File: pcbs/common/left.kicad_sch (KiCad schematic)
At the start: 89 parts, among them J2 TRS

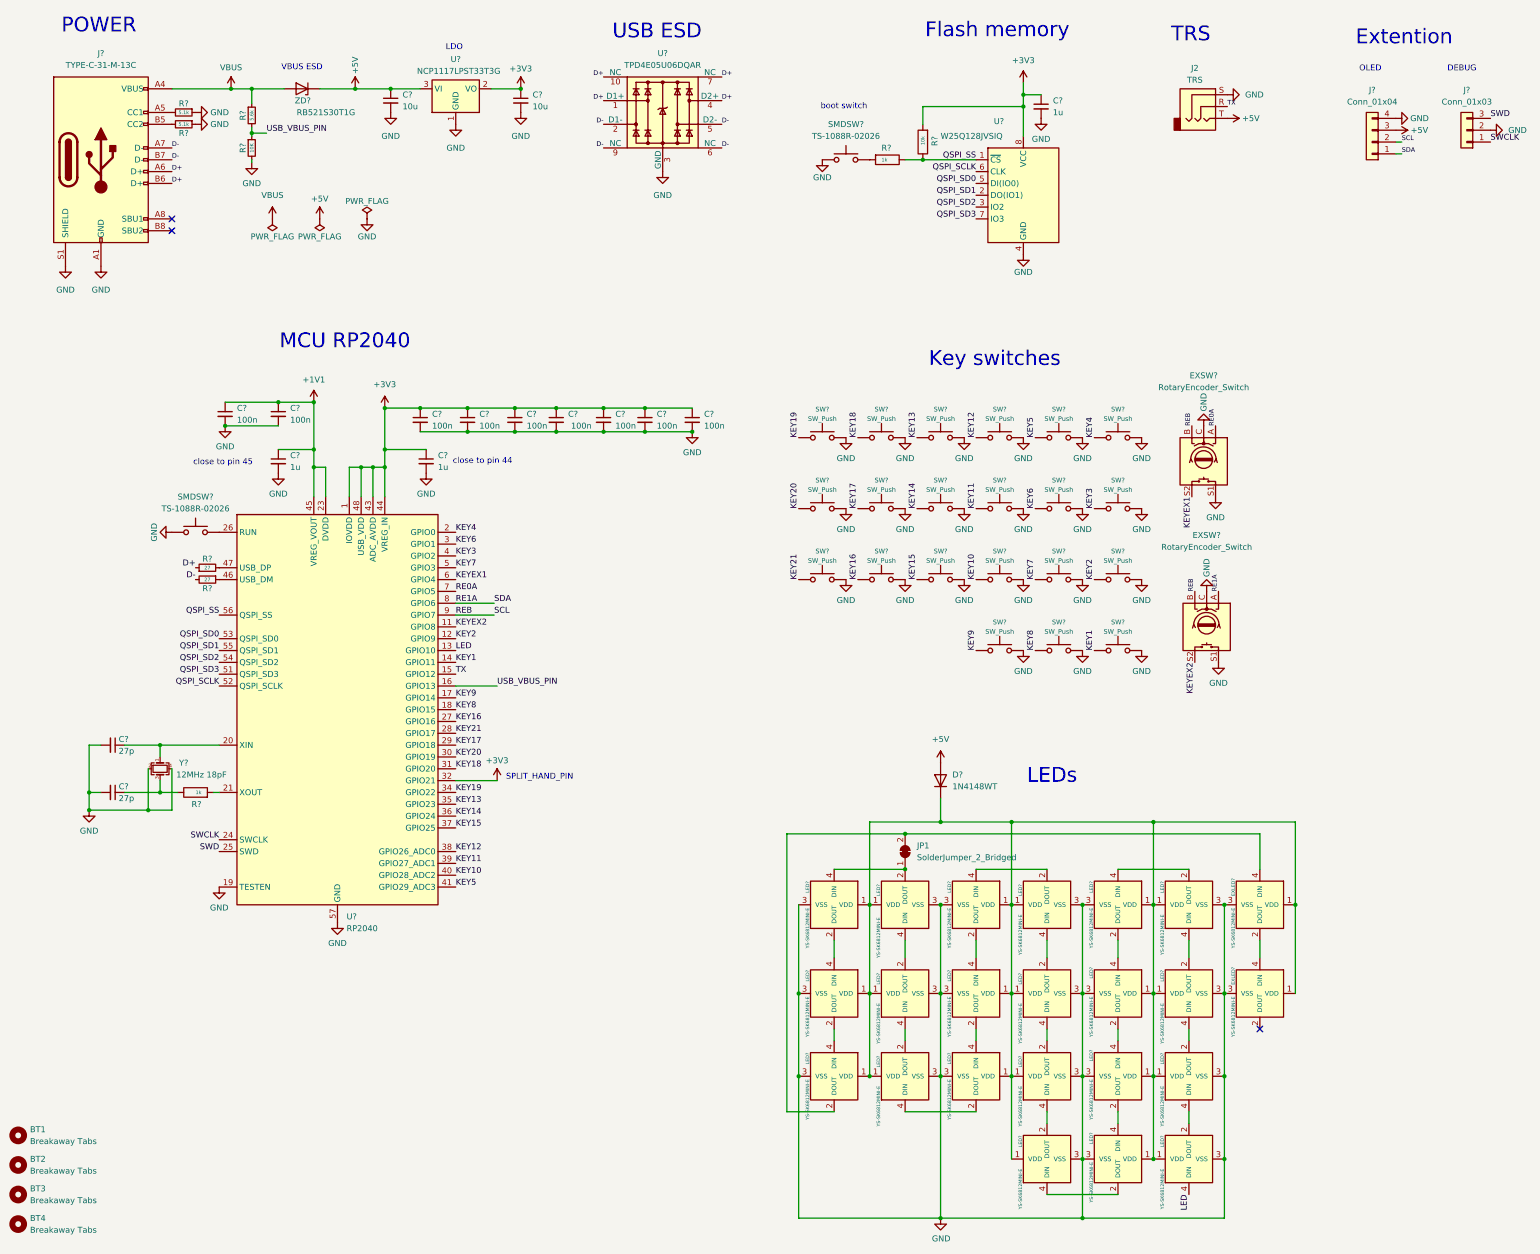
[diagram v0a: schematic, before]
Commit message: KiCad v9
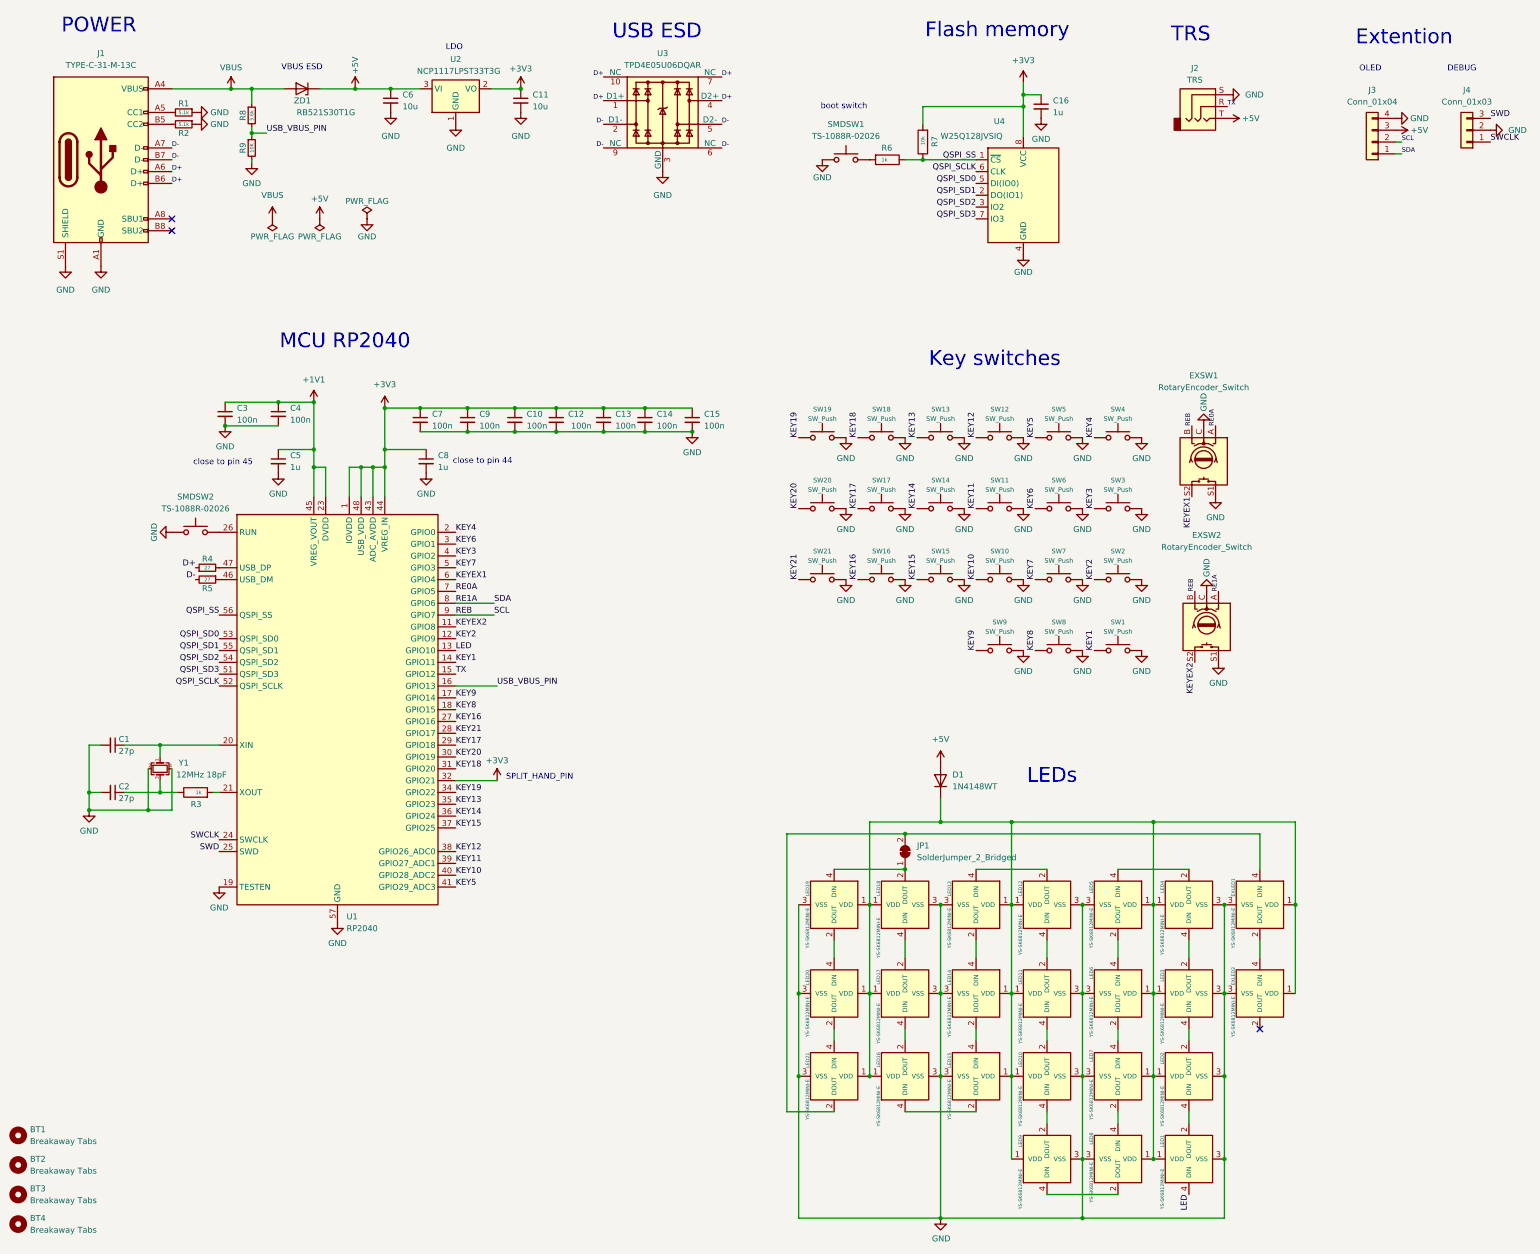
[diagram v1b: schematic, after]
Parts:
- gave numbers to parts that had none: 83

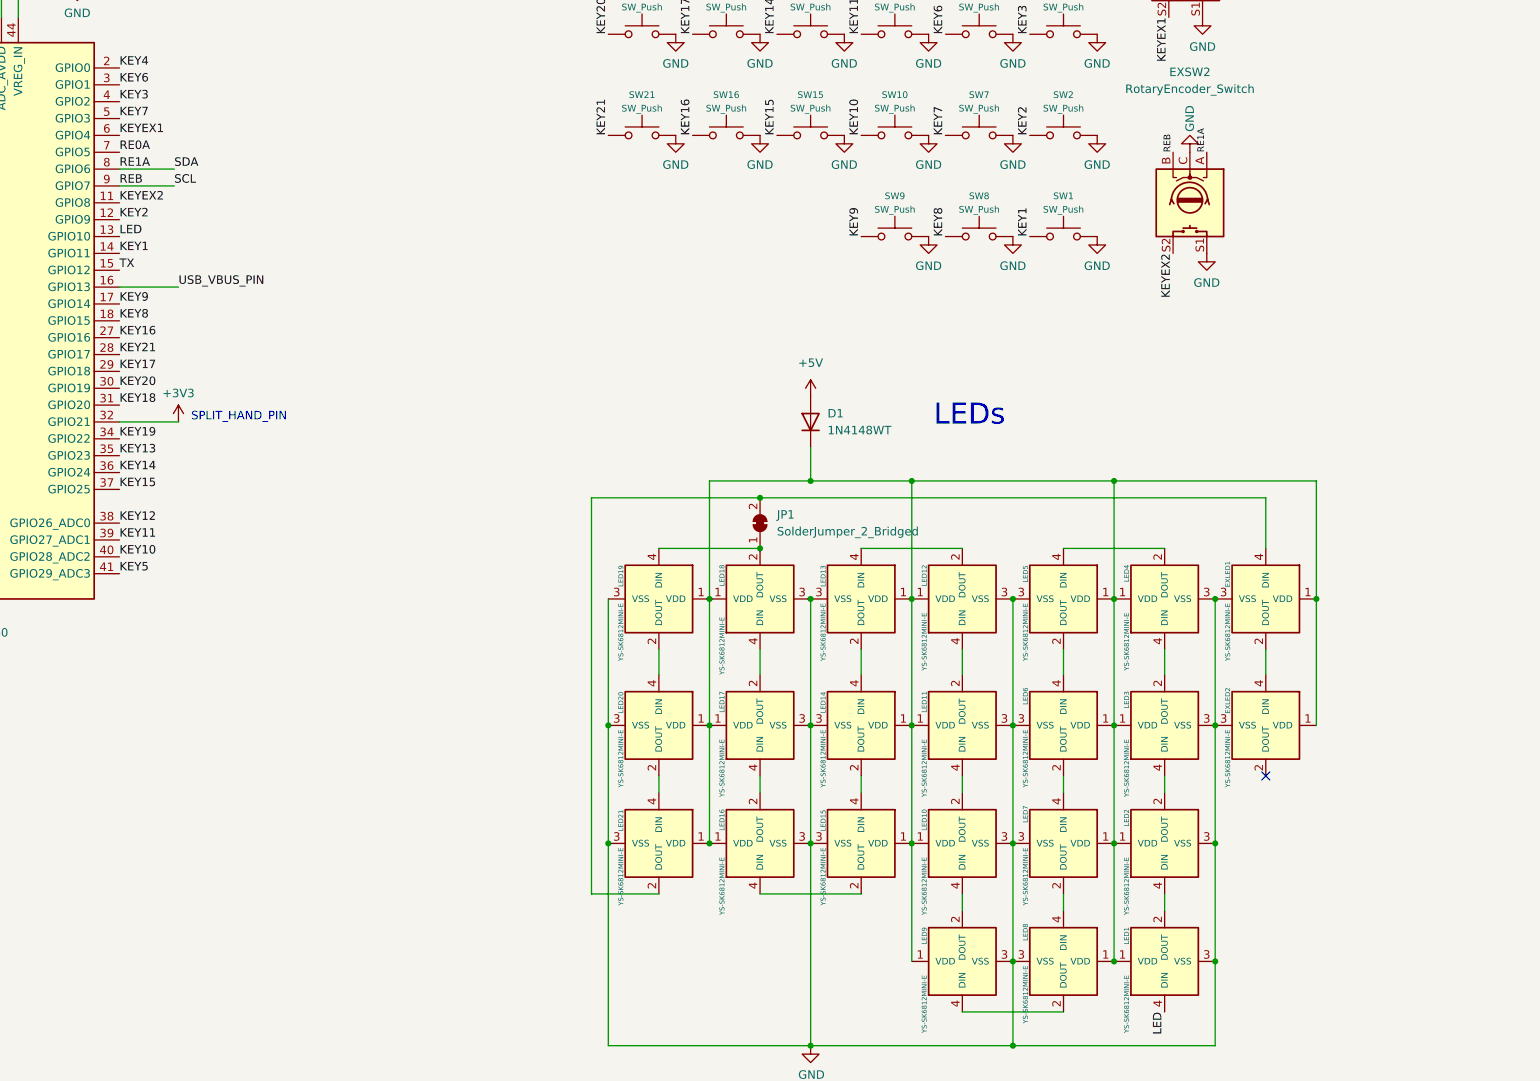
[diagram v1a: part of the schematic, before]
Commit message: add keys and LEDs
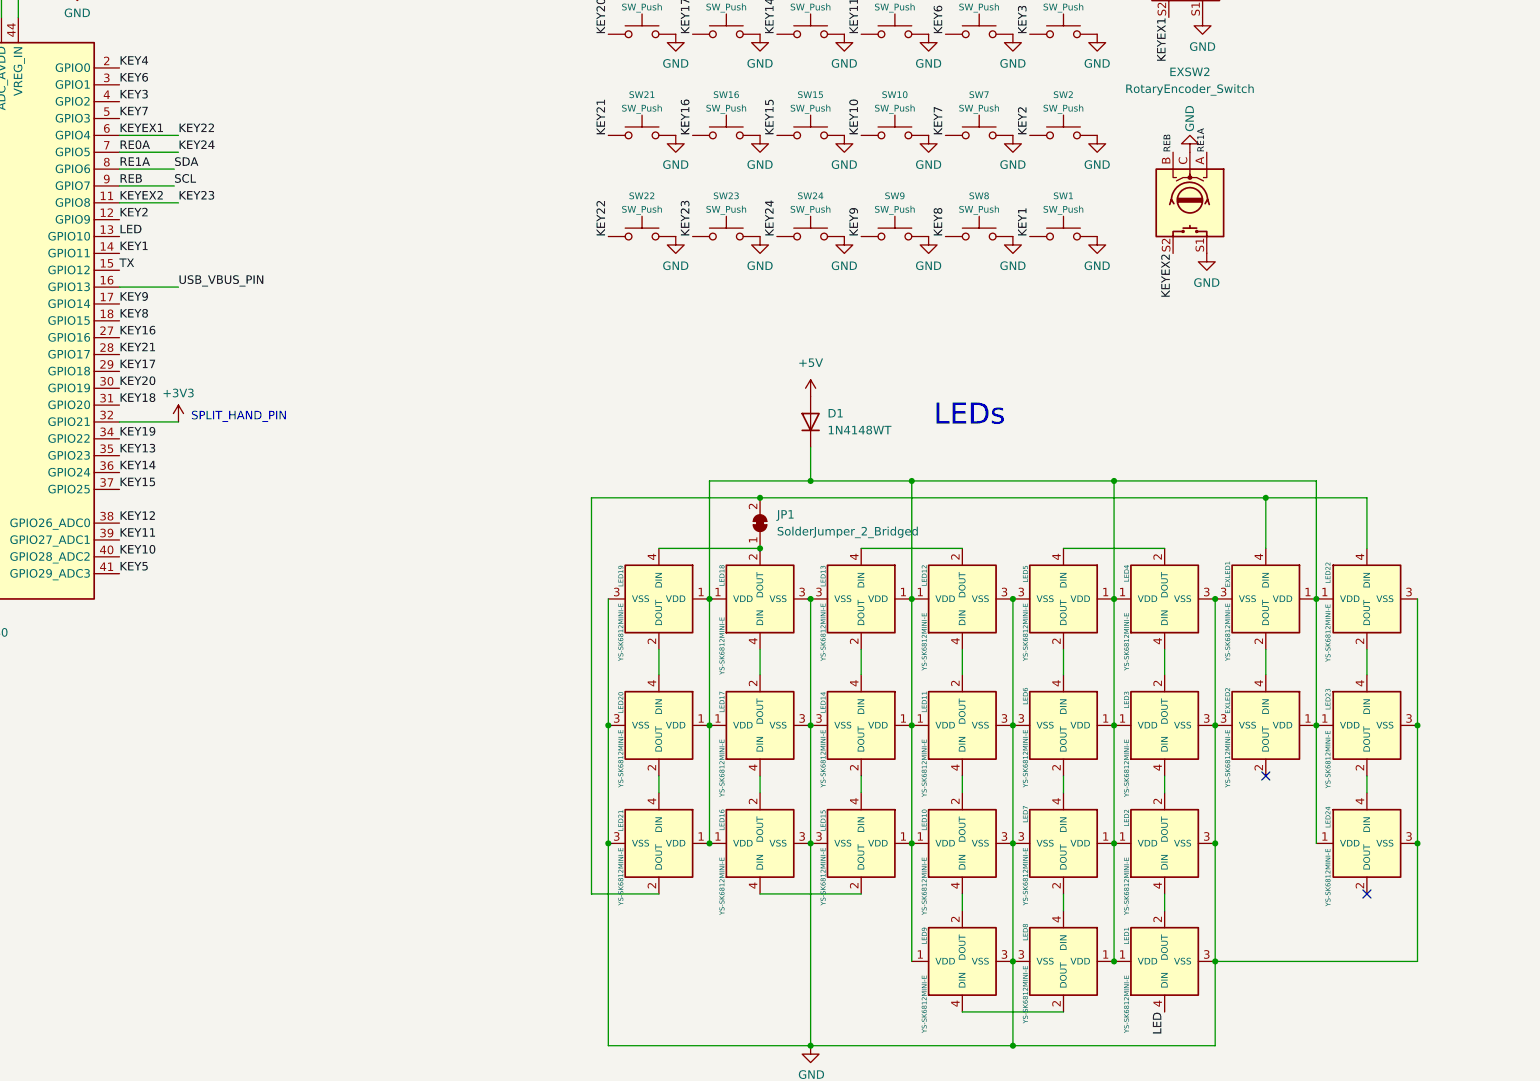
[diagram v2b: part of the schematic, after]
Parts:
- added LED22, LED23, LED24: YS-SK6812MINI-E, kbd_local:YS-SK6812MINI-E, symbol kbd_local:YS-SK6812MINI-E
- added SW22, SW23, SW24: SW_Push, kbd:keyswitch_cherrymx_hotswap_1u, symbol Switch:SW_Push
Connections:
- net GND: now also LED22.3 (VSS), LED23.3 (VSS), LED24.3 (VSS), SW22.2, SW23.2, SW24.2
- net at D1.1 (K), EXLED1.1 (VDD), EXLED2.1 (VDD)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: now also LED22.1 (VDD), LED23.1 (VDD), LED24.1 (VDD)
- net at EXLED1.4 (DIN), JP1.2 (B), LED21.2 (DOUT): now also LED22.4 (DIN)
- net KEYEX1 renamed KEY22
- net KEY22: now also SW22.1
- net KEYEX2 renamed KEY23
- net KEY23: now also SW23.1
- net RE0A renamed KEY24
- net KEY24: now also SW24.1
- new net: LED23.2 (DOUT), LED24.4 (DIN)
- new net: LED22.2 (DOUT), LED23.4 (DIN)
- no-connect marks 3 -> 4
